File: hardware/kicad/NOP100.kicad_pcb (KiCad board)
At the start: 4 copper layers, 100 x 85 mm, 52 parts, among them CON1 MIKROBUS_MODULE_CONN, CON2 MIKROBUS_MODULE_CONN, J1 CAN, Q1 BSS138, Q2 BSS138, SW1 BUS, SW2 SW_Push, U1 MURATA_MEJ2*, U2 MCP2551-I-P, U3 Teensy_4.0, U4 74HC165, U6 NCS1S1203SC

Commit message: Lots of tweaks
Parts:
- CON1: value MIKROBUS_MODULE_CONN -> CLICK MODULE 0
- CON2: value MIKROBUS_MODULE_CONN -> CLICK MODULE 1
- L1, L2: footprint pdjr:TCK_059 -> Inductor_SMD:L_Bourns_SRU5016_5.2x5.2mm
- R6: footprint Resistor_THT:R_Axial_DIN0207_L6.3mm_D2.5mm_P7.62mm_Horizontal -> Resistor_SMD:R_1206_3216Metric
- SW2: footprint Button_Switch_SMD:SW_Push_1P1T_NO_Vertical_Wuerth_434133025816 -> Button_Switch_SMD:SW_SPST_PTS810
- U4: footprint Package_SO:SO-16_3.9x9.9mm_P1.27mm -> Package_SO:SOIC-16_3.9x9.9mm_P1.27mm
- moved C4 2.77 mm to (33.3, -27.3), turned to 0 degrees
- moved L2 1.50 mm to (-44.0, 17.7)
- moved R6 0.95 mm to (-40.0, -30.4)
- moved U4 0.14 mm to (37.4, -22.5)
- moved C5 0.11 mm to (-42.5, -4.70)
- moved L1 0.08 mm to (-44.0, 1.94)
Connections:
- CON1 pad P13: unconnected-(CON1-RX-PadP13) -> /RX
- CON1 pad P14: unconnected-(CON1-TX-PadP14) -> /TX
- CON1 pad P2: /RST0 -> /RST
- CON2 pad P13: unconnected-(CON2-RX-PadP13) -> /RX
- CON2 pad P14: unconnected-(CON2-TX-PadP14) -> /TX
- CON2 pad P2: /RST1 -> /RST
- U3 pad 11: /RST1 -> /PWM1
- U3 pad 2: /EN0 -> /RX
- U3 pad 3: /RST0 -> /TX
- U3 pad 4: /CS0 -> /INT0
- U3 pad 5: /INT0 -> /PWM0
- U3 pad 6: /PWM0 -> /EN0
- U3 pad 7: unconnected-(U3-D5-Pad7) -> /RST
- U3 pad 8: /INT1 -> /CS0
- U3 pad 9: /PWM1 -> /INT1
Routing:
- net /RST: track 0.00 -> 81.6 mm, vias 0 -> 3
- net /TX: track 0.00 -> 71.1 mm, vias 0 -> 3
- net /RX: track 0.00 -> 64.6 mm, vias 0 -> 3
- net /RST1: track 41.0 -> 0.00 mm, vias 2 -> 0
- net /RST0: track 30.2 -> 0.00 mm
- net +3V3: track 39.2 -> 55.6 mm
- net /CS0: track 36.5 -> 42.5 mm, vias 0 -> 2
- net /INT1: track 34.2 -> 30.2 mm, vias 2 -> 0
- net Net-(J1-Pin_4): track 18.4 -> 22.2 mm
- net GND: track 49.7 -> 46.0 mm, vias 12 -> 13
- net Net-(R6-Pad2): track 4.39 -> 8.02 mm
- net /PWM1: track 35.6 -> 32.1 mm, vias 2 -> 0
- net /PWM0: track 48.0 -> 45.5 mm
- net /INT0: track 43.5 -> 41.0 mm
- net /EN0: track 33.8 -> 36.0 mm, vias 0 -> 2
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
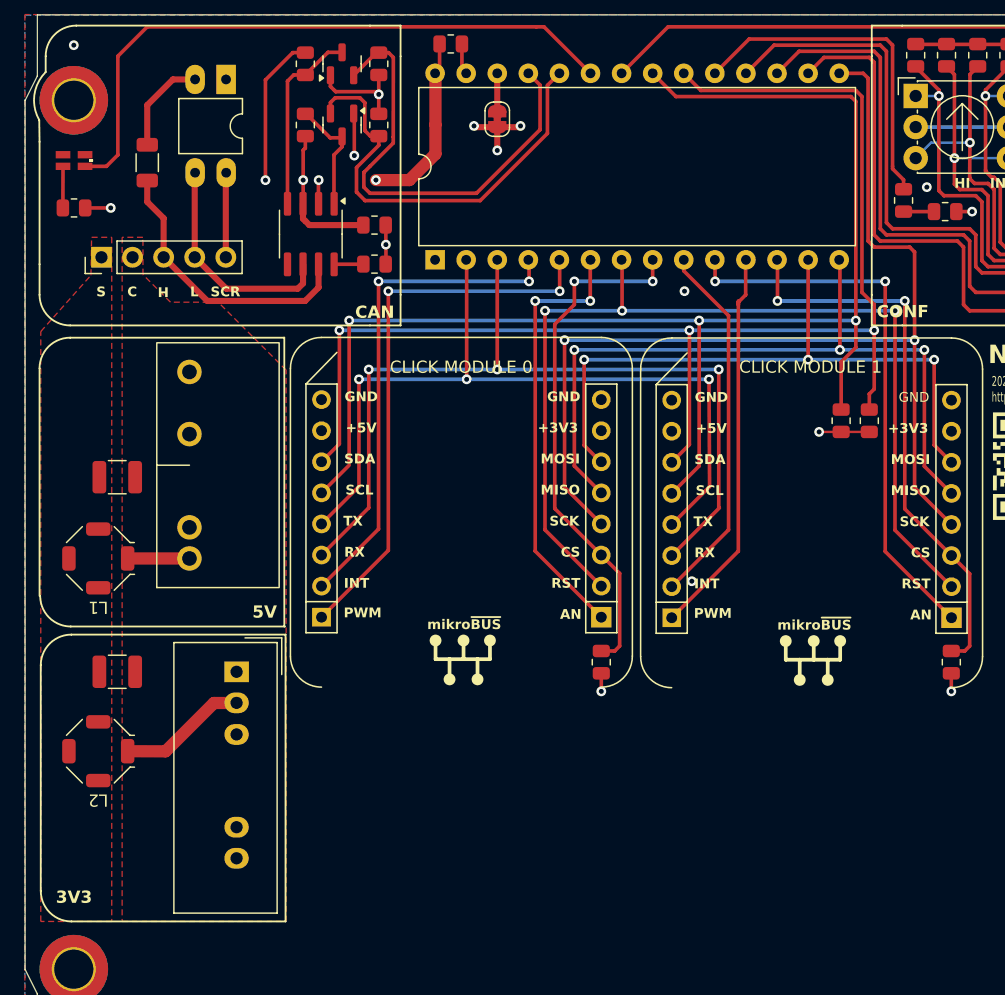
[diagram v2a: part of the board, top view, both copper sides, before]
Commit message: Update GPIO assignments.
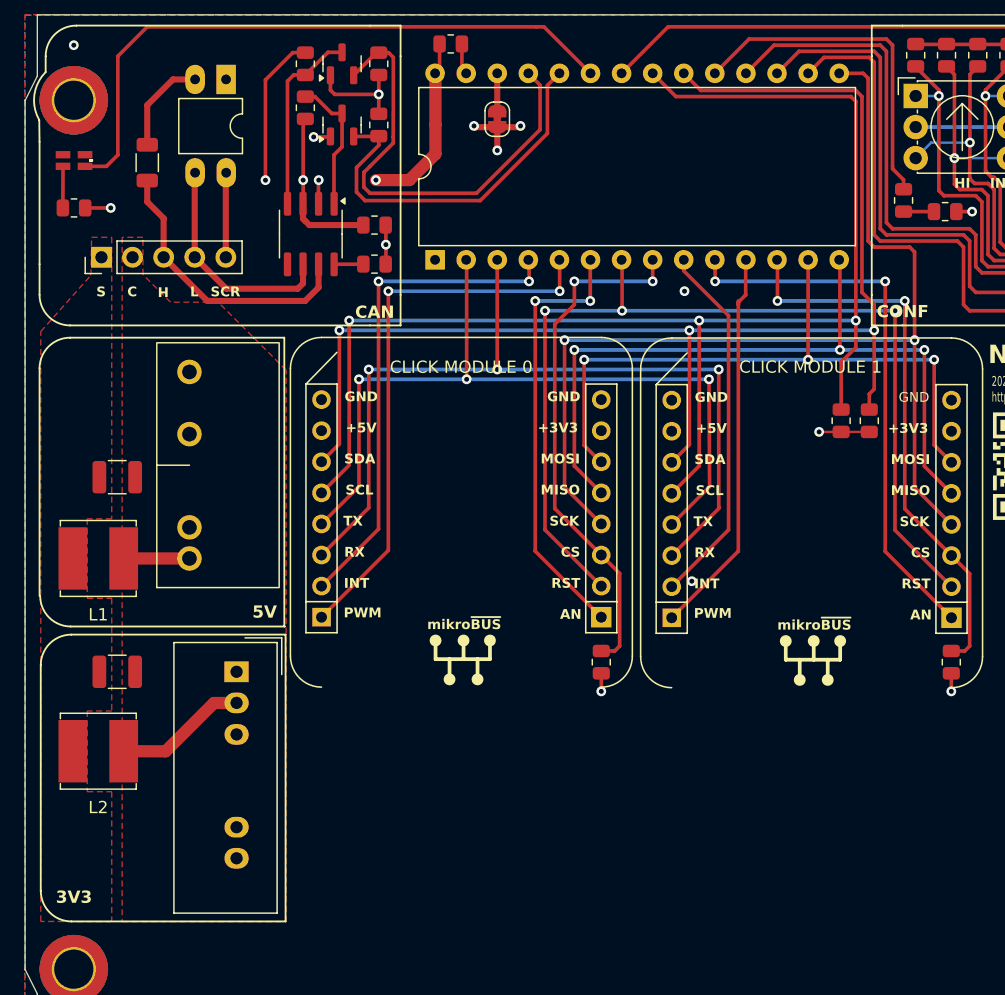
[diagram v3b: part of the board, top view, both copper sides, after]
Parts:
- C5: value 10uF -> 22uF
- L1: value 22uH -> 15uH; footprint Inductor_SMD:L_Bourns_SRU5016_5.2x5.2mm -> Inductor_SMD:L_Bourns_SRN6045TA
- L2: footprint Inductor_SMD:L_Bourns_SRU5016_5.2x5.2mm -> Inductor_SMD:L_Bourns_SRN6045TA
- moved R3 1.41 mm to (-27.1, -34.9)
- turned Q1 to 90 degrees
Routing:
- net /CAN_TX: track 36.4 -> 30.9 mm
- net +3V3: track 55.6 -> 53.7 mm
- net Net-(Q1-D): track 9.45 -> 11.2 mm
- net +5V: track 39.3 -> 40.7 mm
- net GND: vias 13 -> 12

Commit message: Tweaks
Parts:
- moved R17 10.2 mm to (44.3, -39.9), turned to 0 degrees
- moved SW2 4.18 mm to (45.9, -29.1)
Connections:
- HI1 pad 1: +3V3 -> GND
- LO1 pad 1: +3V3 -> GND
- R10 pad 2: GND -> +3V3
- R11 pad 2: GND -> +3V3
- R12 pad 2: GND -> +3V3
- R13 pad 2: GND -> +3V3
- R14 pad 2: GND -> +3V3
- R15 pad 2: GND -> +3V3
- R16 pad 2: GND -> +3V3
- R9 pad 2: GND -> +3V3
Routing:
- net GND: track 46.0 -> 34.4 mm, vias 12 -> 11
- net +3V3: track 53.7 -> 46.6 mm
- net /PRG_BUTTON: track 67.0 -> 68.2 mm
- net Net-(HI1-D1): track 32.9 -> 34.0 mm

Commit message: New build
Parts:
- added OW0: RS_8971054, pdjr:RS_8971054, F.Cu at (34.0, -11.1)
- added OW1: RS_8971054, pdjr:RS_8971054, F.Cu at (44.0, -11.1)
- added OW2: RS_8971054, pdjr:RS_8971054, F.Cu at (34.0, -1.20)
- added OW3: RS_8971054, pdjr:RS_8971054, F.Cu at (44.0, -1.20)
- added OW4: RS_8971054, pdjr:RS_8971054, F.Cu at (34.0, 8.70)
- added OW5: RS_8971054, pdjr:RS_8971054, F.Cu at (44.0, 8.70)
- added OW6: RS_8971054, pdjr:RS_8971054, F.Cu at (34.0, 18.6)
- added OW7: RS_8971054, pdjr:RS_8971054, F.Cu at (44.0, 18.6)
- added REF**: PinHeader_2x05_P2.54mm_Vertical, Connector_PinHeader_2.54mm:PinHeader_2x05_P2.54mm_Vertical, F.Cu at (19.2, 18.2)
- moved G*** 58.0 mm to (-14.3, 27.3)
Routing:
- net (no net): track 0.00 -> 441.6 mm
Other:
- board text added: "GND"
- board text added: "OW0"
- board text added: "OW1"
- board text added: "OW2"
- board text added: "OW3"
- board text added: "OW4"
- board text added: "OW5"
- board text added: "OW6"
- board text added: "OW7"
- board text added: "VCC"

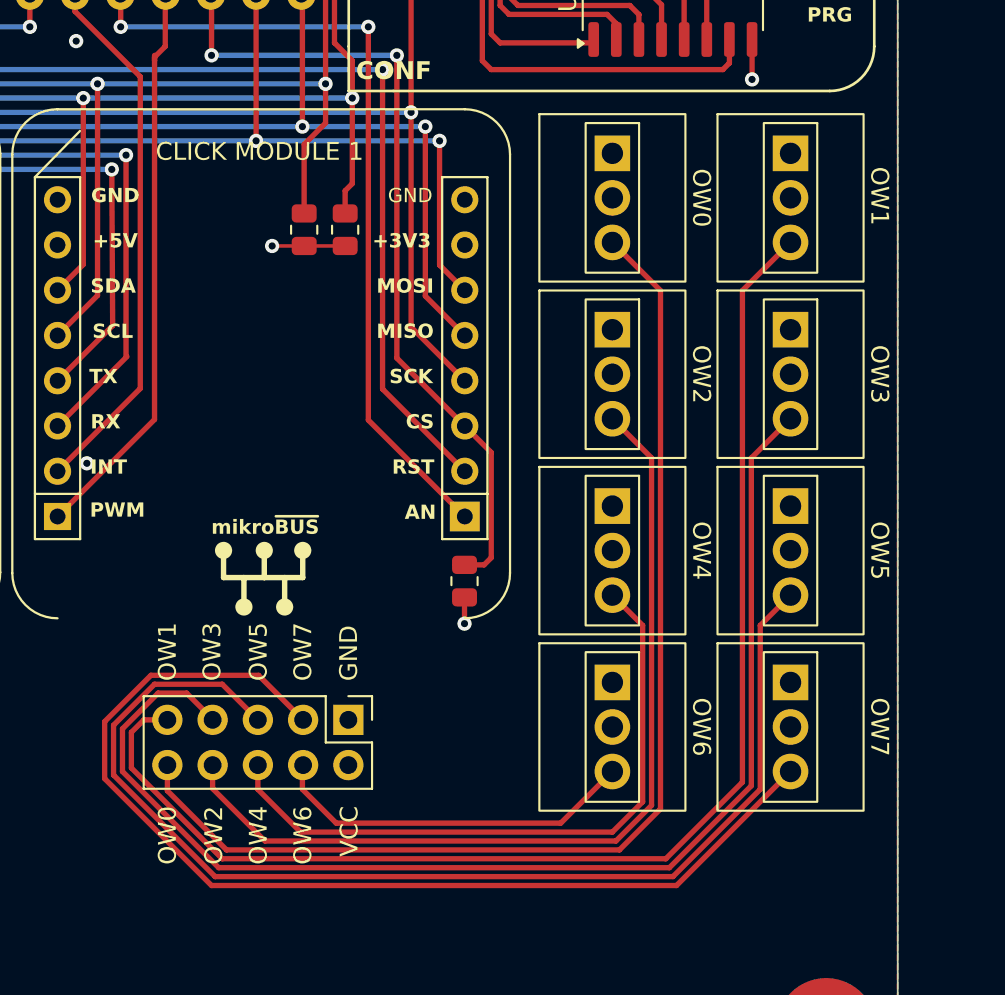
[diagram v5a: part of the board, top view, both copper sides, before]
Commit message: Add 1-wire support
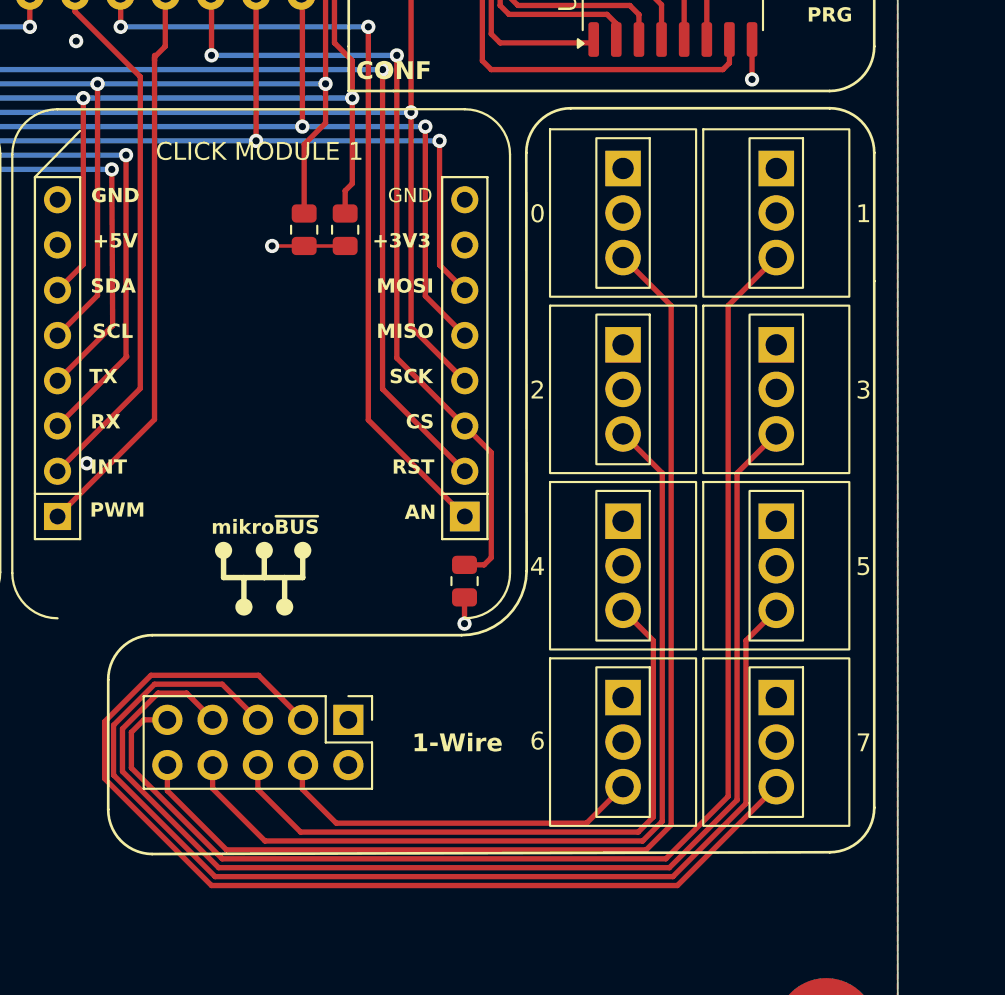
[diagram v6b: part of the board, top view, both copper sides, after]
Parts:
- moved OW5 1.17 mm to (43.2, 9.55)
- moved OW3 1.17 mm to (43.2, -0.35)
- moved OW1 1.17 mm to (43.2, -10.2)
- moved OW7 1.17 mm to (43.2, 19.4)
- moved OW4 1.04 mm to (34.6, 9.55)
- moved OW2 1.04 mm to (34.6, -0.35)
- moved OW0 1.04 mm to (34.6, -10.2)
- moved OW6 1.04 mm to (34.6, 19.4)
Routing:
- net (no net): track 441.6 -> 437.9 mm
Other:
- board text added: "0"
- board text added: "1"
- board text added: "1-Wire"
- board text added: "2"
- board text added: "3"
- board text added: "4"
- board text added: "5"
- board text added: "6"
- board text added: "7"
- board text removed: "GND"
- board text removed: "OW0"
- board text removed: "OW1"
- board text removed: "OW2"
- board text removed: "OW3"
- board text removed: "OW4"
- board text removed: "OW5"
- board text removed: "OW6"
- board text removed: "OW7"
- board text removed: "VCC"

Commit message: Tweaks
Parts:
- removed OW0, OW1, OW2, OW3, OW4, OW5, OW6, OW7: RS_8971054, pdjr:RS_8971054
- removed the REF** at (19.2, 18.2)
- added J10: Conn_01x03, pdjr:RS_8971054, F.Cu at (43.2, 19.4)
- added J2: Conn_01x03, pdjr:RS_8971054, F.Cu at (34.6, -0.35)
- added J3: Conn_01x03, pdjr:RS_8971054, F.Cu at (34.6, -10.2)
- added J4: Conn_01x03, pdjr:RS_8971054, F.Cu at (34.6, 9.55)
- added J5: Conn_01x03, pdjr:RS_8971054, F.Cu at (34.6, 19.4)
- added J6: Conn_01x03, pdjr:RS_8971054, F.Cu at (43.2, -10.2)
- added J7: Conn_02x05_Odd_Even, Connector_PinSocket_2.54mm:PinSocket_2x05_P2.54mm_Vertical, F.Cu at (19.2, 20.7)
- added J8: Conn_01x03, pdjr:RS_8971054, F.Cu at (43.2, -0.35)
- added J9: Conn_01x03, pdjr:RS_8971054, F.Cu at (43.2, 9.55)
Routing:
- net (no net): track 437.9 -> 0.00 mm
- net /OW_VCC: track 0.00 -> 93.0 mm, vias 0 -> 1
- net /OW_GND: track 0.00 -> 92.8 mm
- net /OW1: track 0.00 -> 72.6 mm
- net /OW3: track 0.00 -> 68.8 mm
- net /OW0: track 0.00 -> 64.8 mm
- net /OW5: track 0.00 -> 64.0 mm
- net /OW7: track 0.00 -> 59.3 mm
- net /OW2: track 0.00 -> 51.0 mm
- net /OW4: track 0.00 -> 37.2 mm
- net /OW6: track 0.00 -> 21.0 mm

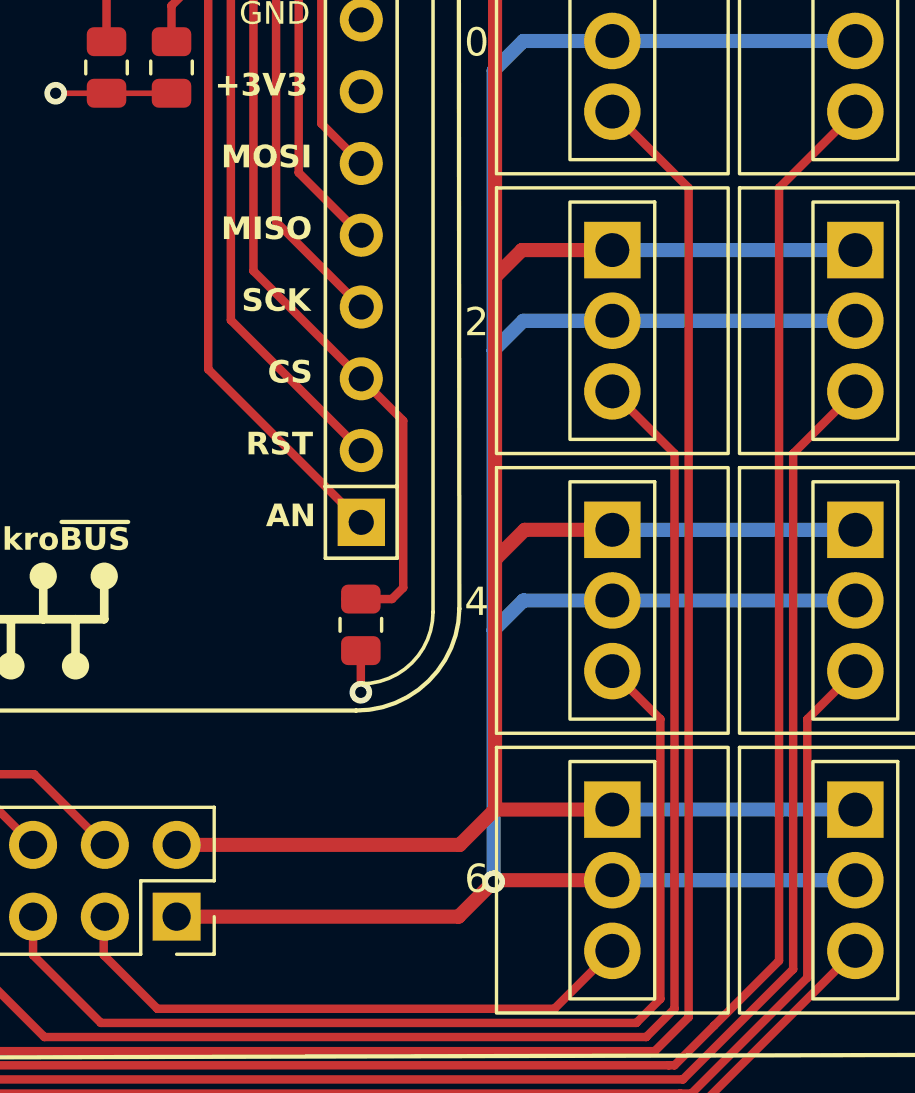
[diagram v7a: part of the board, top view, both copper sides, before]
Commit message: Adjust fill zones.
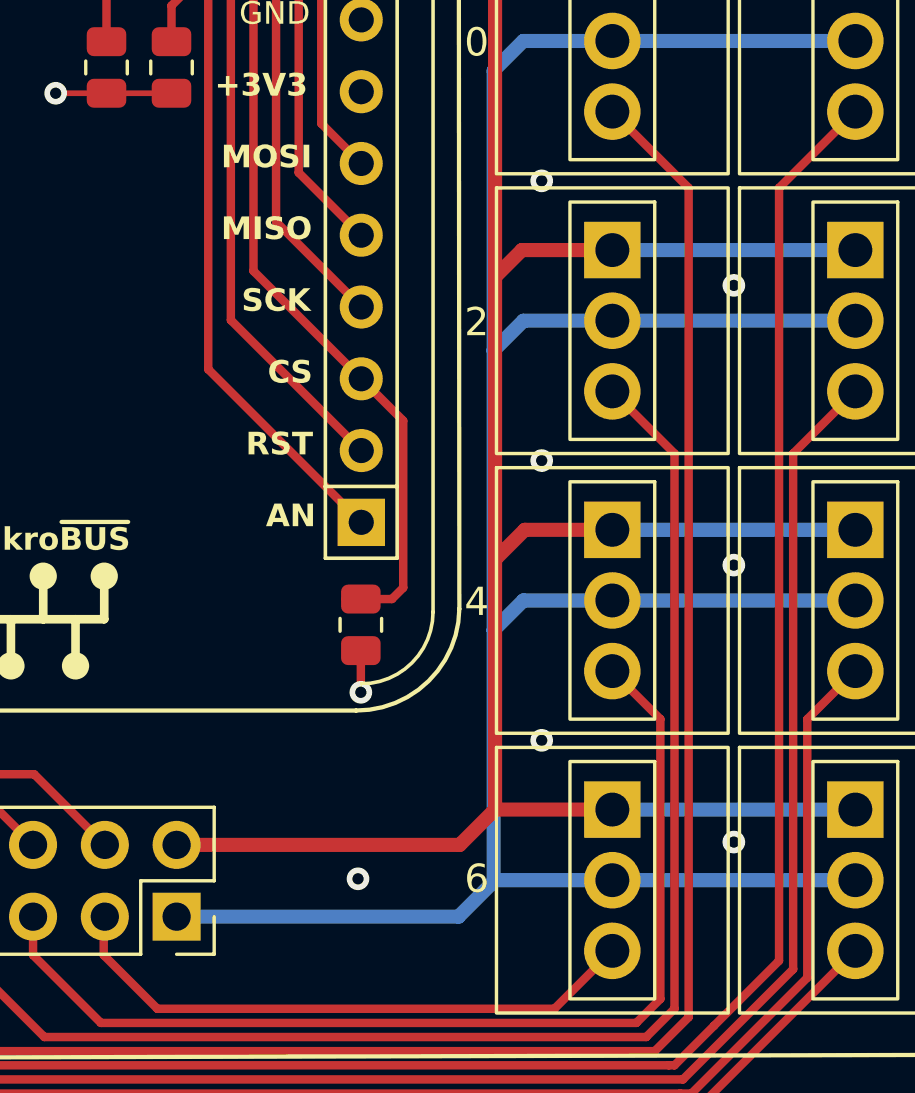
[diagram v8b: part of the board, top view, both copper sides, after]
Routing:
- net /OW_VCC: track 93.0 -> 92.9 mm, vias 1 -> 0
- net GND: vias 11 -> 18
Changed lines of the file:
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@@
   (segment (start -20.495 -22.11) (end -20.495 -23.695) (width 0.3) (layer "F.Cu") (net 1))
   (via (at -42.981 -26.7) (size 0.8) (drill 0.4) (layers "F.Cu" "B.Cu") (net 1))
+  (via (at 38.9 -1.6) (size 0.8) (drill 0.4) (layers "F.Cu" "B.Cu") (free) (net 1))
   (via (at 41.84 -17.75) (size 0.8) (drill 0.4) (layers "F.Cu" "B.Cu") (net 1))
   (via (at 4.5 3.8) (size 0.8) (drill 0.4) (layers "F.Cu" "B.Cu") (free) (net 1))
   (via (at 32 -31.9) (size 0.8) (drill 0.4) (layers "F.Cu" "B.Cu") (net 1))
   (via (at 34.2 -28.8) (size 0.8) (drill 0.4) (layers "F.Cu" "B.Cu") (net 1))
+  (via (at 32.1 4.6) (size 0.8) (drill 0.4) (layers "F.Cu" "B.Cu") (free) (net 1))
   (via (at 40.57 -26.979) (size 0.8) (drill 0.4) (layers "F.Cu" "B.Cu") (net 1))
   (via (at -46.7 -40.2) (size 0.8) (drill 0.4) (layers "F.Cu" "B.Cu") (free) (net 1))
+  (via (at 38.9 8.3) (size 0.8) (drill 0.4) (layers "F.Cu" "B.Cu") (free) (net 1))
+  (via (at 38.9 18.1) (size 0.8) (drill 0.4) (layers "F.Cu" "B.Cu") (free) (net 1))
   (via (at -20.5 -23.7) (size 0.8) (drill 0.4) (layers "F.Cu" "B.Cu") (free) (net 1))
   (via (at 27.4 -26.4) (size 0.8) (drill 0.4) (layers "F.Cu" "B.Cu") (net 1))
   (via (at 3.9 -19.9) (size 0.8) (drill 0.4) (layers "F.Cu" "B.Cu") (free) (net 1))
+  (via (at 32.1 -5.3) (size 0.8) (drill 0.4) (layers "F.Cu" "B.Cu") (free) (net 1))
+  (via (at 32.1 14.5) (size 0.8) (drill 0.4) (layers "F.Cu" "B.Cu") (free) (net 1))
+  (via (at 25.6 19.4) (size 0.8) (drill 0.4) (layers "F.Cu" "B.Cu") (free) (net 1))
   (via (at -25.988 -28.976) (size 0.8) (drill 0.4) (layers "F.Cu" "B.Cu") (net 1))
   (segment (start -16.45 -37.67) (end -16.48 -37.7) (width 1) (layer "F.Cu") (net 2))
@@
   (segment (start 34.6 -12.75) (end 43.2 -12.75) (width 0.5) (layer "B.Cu") (net 63))
   (segment (start 34.6 16.95) (end 43.2 16.95) (width 0.5) (layer "B.Cu") (net 63))
-  (segment (start 30.45 19.45) (end 30.4 19.5) (width 0.5) (layer "F.Cu") (net 64))
-  (segment (start 30.4 19.5) (end 29.16 20.74) (width 0.5) (layer "F.Cu") (net 64))
-  (segment (start 29.16 20.74) (end 19.18 20.74) (width 0.5) (layer "F.Cu") (net 64))
-  (segment (start 34.6 19.45) (end 30.45 19.45) (width 0.5) (layer "F.Cu") (net 64))
-  (via (at 30.4 19.5) (size 0.8) (drill 0.4) (layers "F.Cu" "B.Cu") (net 64))
   (segment (start 30.4 0.7) (end 30.4 -9.2) (width 0.5) (layer "B.Cu") (net 64))
   (segment (start 34.6 9.55) (end 31.45 9.55) (width 0.5) (layer "B.Cu") (net 64))
+  (segment (start 30.4 19.5) (end 29.16 20.74) (width 0.5) (layer "B.Cu") (net 64))
+  (segment (start 29.16 20.74) (end 19.18 20.74) (width 0.5) (layer "B.Cu") (net 64))
+  (segment (start 34.6 19.45) (end 30.45 19.45) (width 0.5) (layer "B.Cu") (net 64))
   (segment (start 30.4 10.6) (end 30.4 0.7) (width 0.5) (layer "B.Cu") (net 64))
   (segment (start 30.4 19.5) (end 30.4 10.6) (width 0.5) (layer "B.Cu") (net 64))
